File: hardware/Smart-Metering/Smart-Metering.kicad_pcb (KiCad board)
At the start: 4 copper layers, 130 x 130 mm, 227 parts, among them J101 AUX L N, J201 VA VB VC VN, J301 SENSOR_IA, J302 SENSOR_IB, J303 SENSOR_IC, J304 SENSOR_IN, J501 SWD, J701 HMI_LINK, J801 RS485, J802 USB-C, J901 BATTERY_1S, SW901 POWER, U401 ADE9430ACPZ, U501 STM32F413RHT6, U502 24LC64, U601 ISO7762DW, U602 ISO7761DW, U604 MCP3204, U605 TPS7A2033PDBVR, U606 ADuM6000, U801 ADM2587E, U802 USBLC6-2SC6, U901 BQ25895RTW, U902 TPS63001, U903 TPS61022, Y401 24.576MHz, Y501 8MHz, Y502 32.768kHz

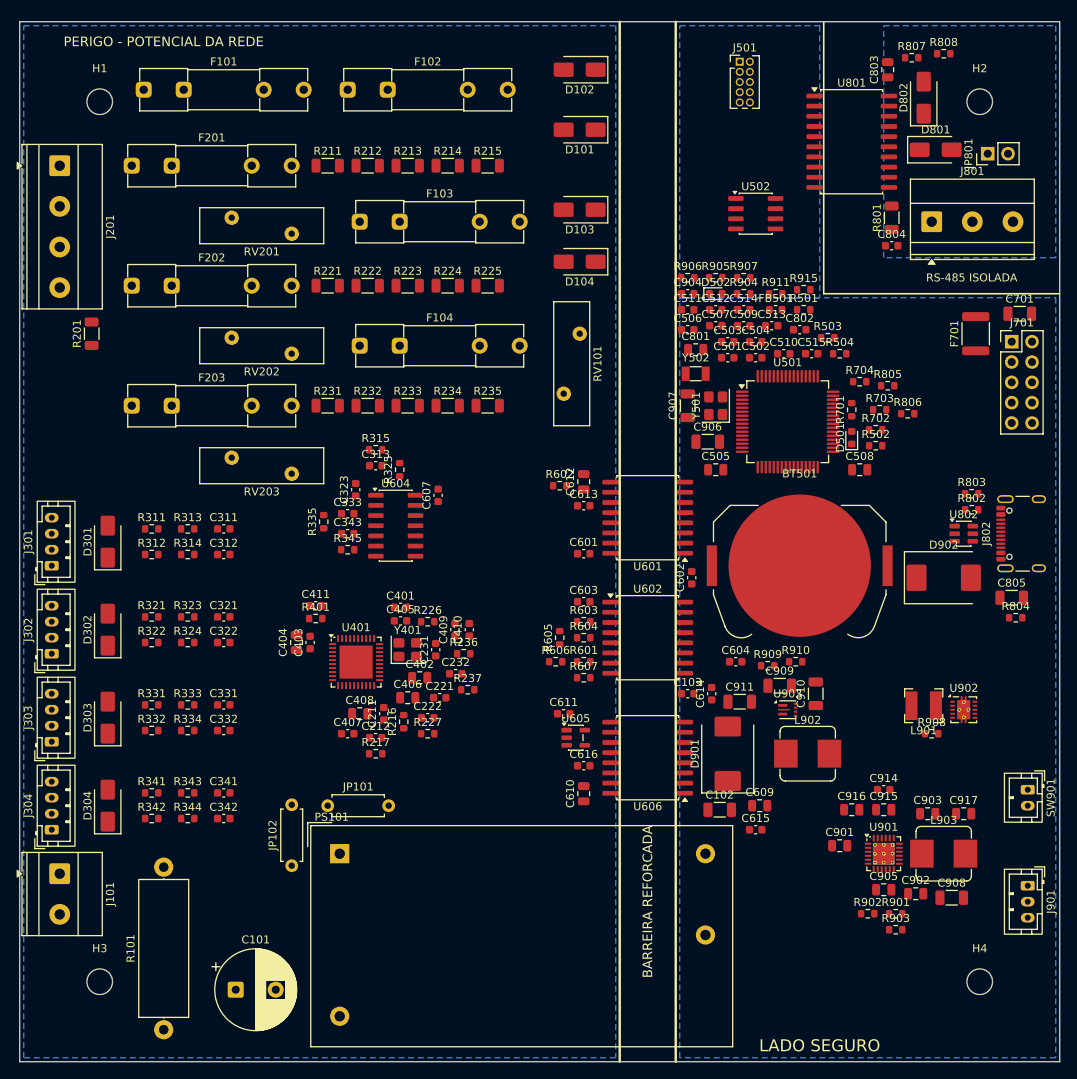
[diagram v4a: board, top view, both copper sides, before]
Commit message: Grava as trilhas e vias do domínio quente na placa
O commit anterior registrou só a documentação; este inclui o roteamento
(3836 trilhas, 139 vias e a zona +3V3_ADE em In2.Cu).

Co-Authored-By: Claude Opus 5.5 <noreply@anthropic.com>
Claude-Session: https://claude.ai/code/session_012B8cVkhtjf3eg98UdpNCpf
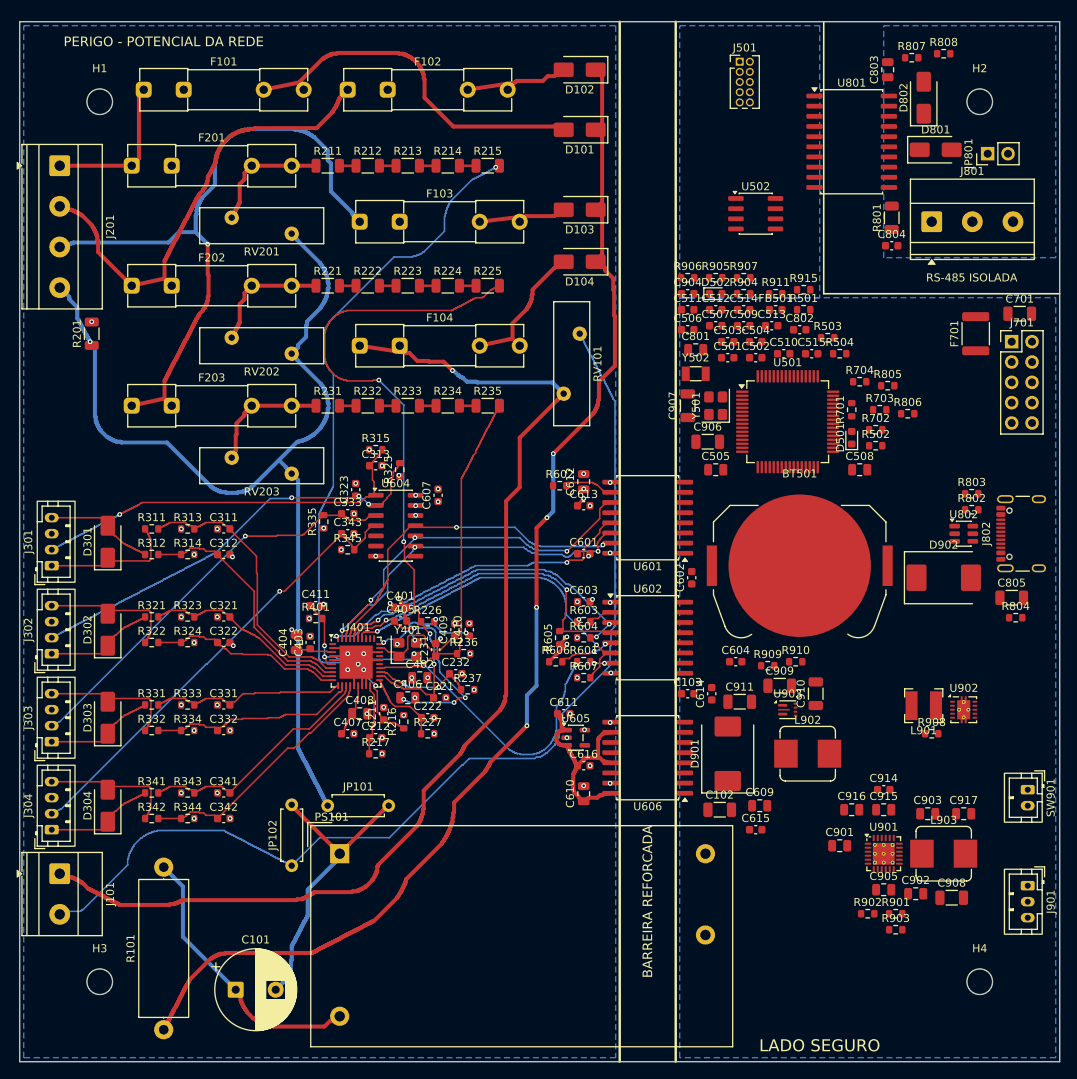
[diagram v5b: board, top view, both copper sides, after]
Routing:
- net Net-(D101-Pad1): track 0.00 -> 155.5 mm, vias 0 -> 4
- net /Power Input/L_AUX: track 0.00 -> 140.3 mm, vias 0 -> 1
- net /Power Input/N_AUX: track 0.00 -> 131.4 mm
- net NEUTRAL: track 0.00 -> 130.6 mm, vias 0 -> 1
- net VAP: track 0.00 -> 91.1 mm, vias 0 -> 2
- net VBP: track 0.00 -> 86.8 mm, vias 0 -> 4
- net LINE_C: track 0.00 -> 83.6 mm, vias 0 -> 1
- net SID_N: track 0.00 -> 57.6 mm, vias 0 -> 1
- net LINE_B: track 0.00 -> 57.6 mm
- net SID_B: track 0.00 -> 55.0 mm, vias 0 -> 3
- net RESET_ADE: track 0.00 -> 54.3 mm, vias 0 -> 3
- net SID_C: track 0.00 -> 51.9 mm, vias 0 -> 1
- net SID_A: track 0.00 -> 49.8 mm, vias 0 -> 1
- net Net-(D101-Pad2): track 0.00 -> 45.0 mm
- net MISO_ADE: track 0.00 -> 44.7 mm, vias 0 -> 3
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- added copper zone on In2.Cu, net +3V3_ADE

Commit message: Liga parte das pendências do domínio quente e alinha CIs de passo fino
- reparo local (com retirada e refação dos nets que bloqueiam): ligados
  SS_SID (U604.8), IRQ0_ADE (U401.31) e +3V3_ADE em U401.1 e U401.27;
  alguns trechos curtos usam In2.Cu (plano +3V3_ADE) como camada de sinal;
- U501, U901, U902, U903 e J802 deslocados até 0,05 mm para os pads de
  passo 0,5 mm ficarem na grade de roteamento (preparação do lado seguro).

Verificação geométrica do domínio quente: 0 violações.

Co-Authored-By: Claude Opus 5.5 <noreply@anthropic.com>
Claude-Session: https://claude.ai/code/session_012B8cVkhtjf3eg98UdpNCpf
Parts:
- moved U901 0.07 mm to (148.1, 134.1)
- moved U501 0.07 mm to (135.9, 80.0)
- moved J802 0.06 mm to (166.3, 94.0)
- moved U903 0.06 mm to (136.0, 116.0)
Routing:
- net IRQ0_ADE: track 6.18 -> 49.4 mm, vias 0 -> 4
- net /Isolation/SS_SID: track 0.00 -> 25.7 mm, vias 0 -> 4
- net RESET_ADE: track 54.3 -> 46.7 mm, vias 3 -> 4
- net +3V3_ADE: track 7.44 -> 9.71 mm, vias 21 -> 23
- added copper zone on In2.Cu, net +3V3

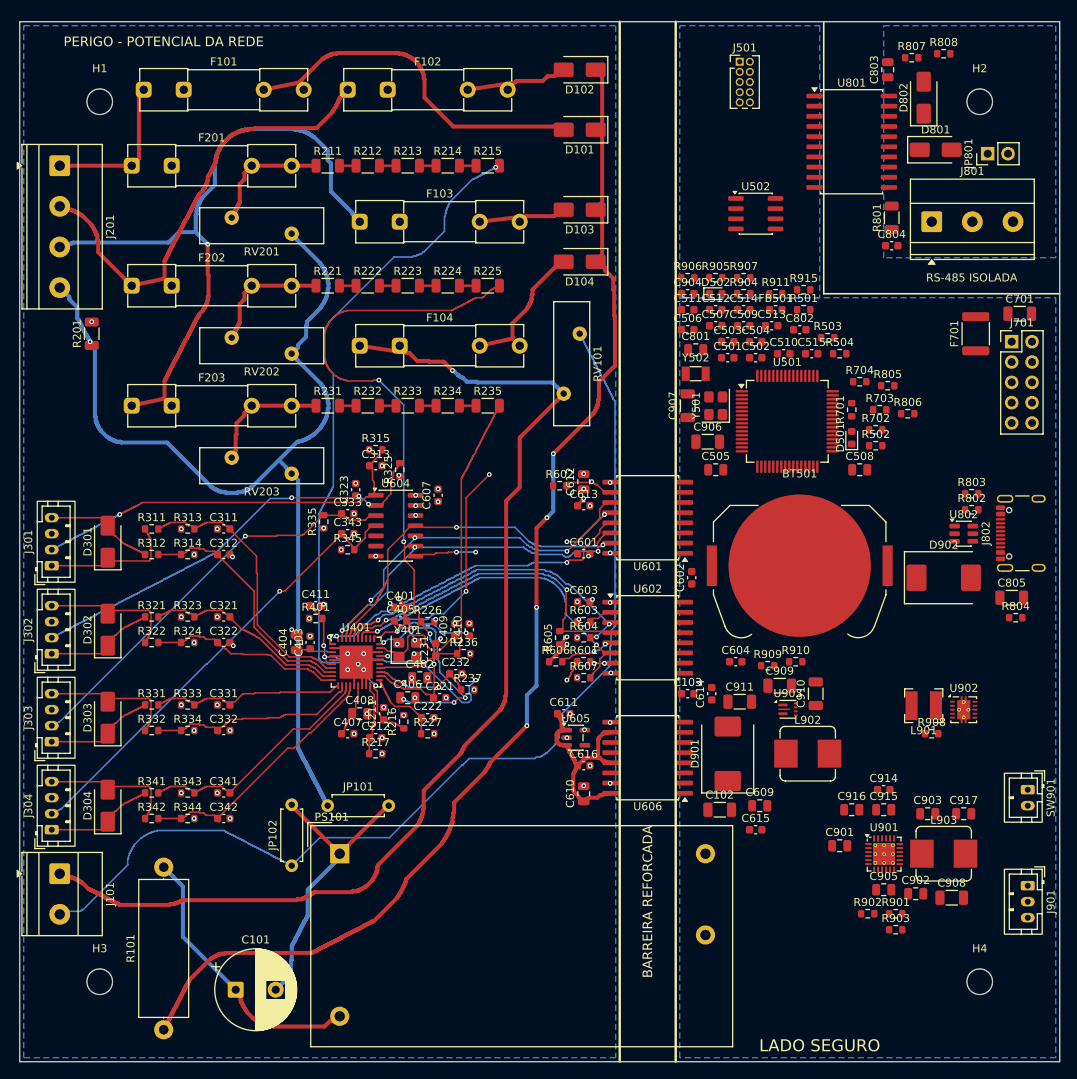
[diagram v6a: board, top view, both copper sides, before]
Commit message: Corrige os achados da revisão automática do PR #1
- BQ25895: divisor do TS invertido (R901 = 5,23 kΩ REGN-TS, R903 = 30,1 kΩ
  TS-GND); antes o carregador via sobretemperatura e não carregava.
- Detecção da fonte: Q902 une D+/D- (DCP, 3 A) só com o AC/DC presente;
  só pelo USB-C a entrada fica em 500 mA. Q901 corta o VBUS quando o AC/DC
  está presente (prioridade do AC/DC sobre a porta USB). R912 polariza os dois.
- DRC: classes DIVIDER_A/B/C, regras entre divisores de fases diferentes
  (3,0 mm), divisor x domínio metrológico (2,0 mm), divisor x rede de outras
  fases (3,0 mm), barramento HV com clearance e creepage, creepage da
  barreira 8,0 mm (com regra própria entre as fileiras dos isoladores).
- Pinos sem uso do lado isolado do U606 classificados no domínio quente.
- Projeto KiCad: folha raiz correta em top_level_sheets.
- PCB: Q901, Q902, R912 posicionados; C103 afastado dos pads quentes de
  U602/U606; zonas com margem para 8 mm na barreira.
- Documentação: ISO7762/ISO7761 na arquitetura, limite de entrada de 3 A
  na revisão, roteamento do domínio quente descrito como parcial.

Co-Authored-By: Claude Opus 5.5 <noreply@anthropic.com>
Claude-Session: https://claude.ai/code/session_012B8cVkhtjf3eg98UdpNCpf
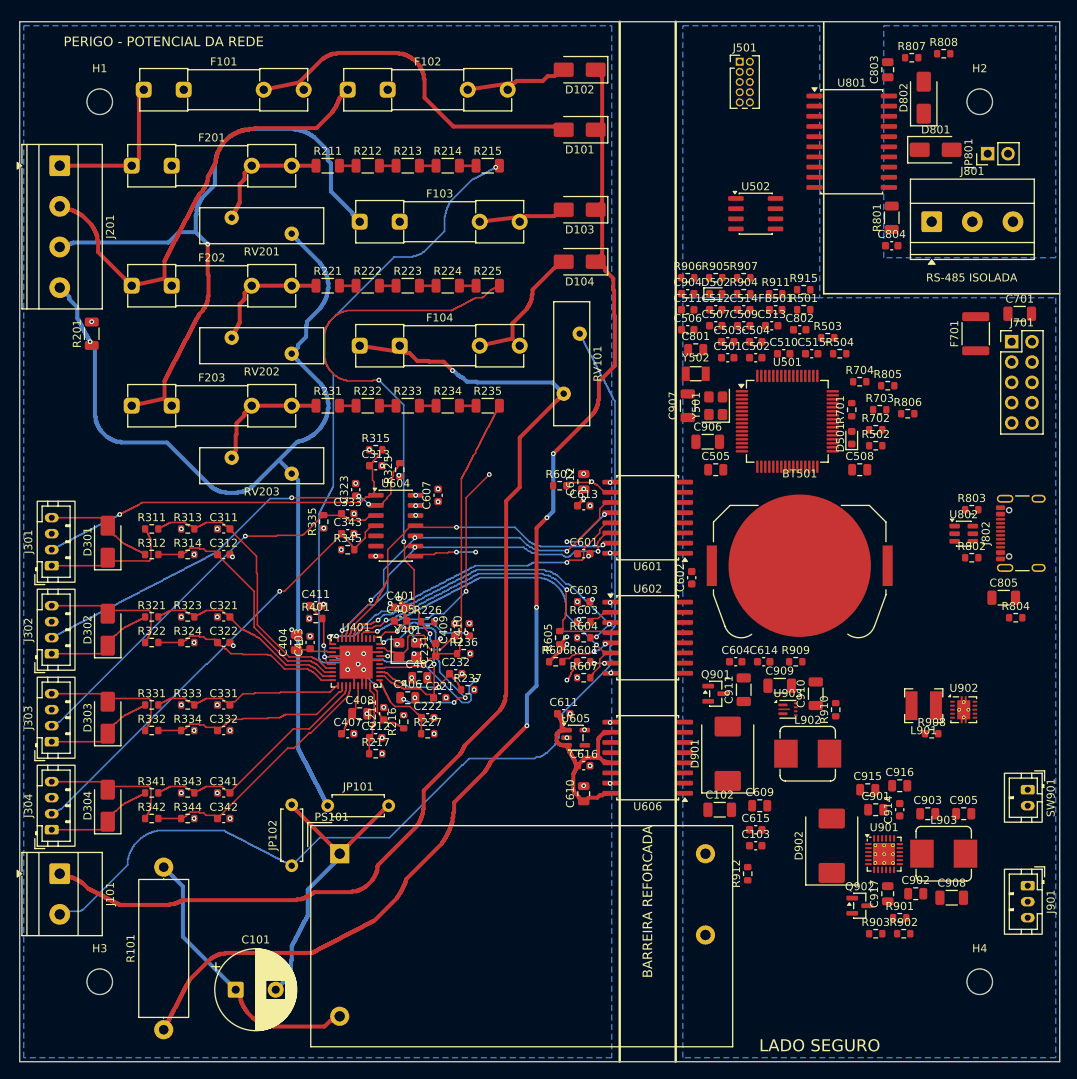
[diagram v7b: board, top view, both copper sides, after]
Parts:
- removed the H1 at (50.0, 40.0)
- added H4: MountingHole_3.2mm_M3, MountingHole:MountingHole_3.2mm_M3, F.Cu at (160.0, 150.0)
- added Q901: AO3401A, Package_TO_SOT_SMD:SOT-23, F.Cu at (127.0, 114.0)
- added Q902: 2N7002, Package_TO_SOT_SMD:SOT-23, F.Cu at (145.0, 140.5)
- added R912: 100k, Resistor_SMD:R_0603_1608Metric, F.Cu at (131.0, 136.5)
- R901: value 30.1k -> 5.23k
- R903: value 5.23k -> 30.1k
- moved H1 155.6 mm to (50.0, 40.0)
- moved D902 36.3 mm to (141.5, 133.0), turned to 90 degrees
- moved C103 20.8 mm to (132.0, 133.0)
- moved C905 13.8 mm to (158.0, 129.0)
- moved C917 13.8 mm to (148.5, 139.0), turned to 90 degrees
- moved R910 7.81 mm to (142.0, 116.0), turned to 90 degrees
- moved C614 7.63 mm to (133.0, 110.0), turned to 0 degrees
- moved C916 6.71 mm to (150.0, 125.5)
- moved C901 6.36 mm to (147.0, 128.5)
- moved R802 6.00 mm to (159.0, 97.0)
- moved R902 5.15 mm to (150.5, 144.0)
- moved R909 3.54 mm to (137.0, 110.0)
- moved C914 3.20 mm to (150.0, 128.5), turned to 90 degrees
- moved C915 3.20 mm to (146.0, 126.0)
- moved R903 2.55 mm to (147.0, 144.0)
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- renumbered H4 to H1
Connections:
- D902 pad 2: VBUS -> /Power Supplies/VBUS_SW
- U901 pad 2: /Power Supplies/CHG_DPDM -> /Power Supplies/CHG_DP
- U901 pad 3: /Power Supplies/CHG_DPDM -> /Power Supplies/CHG_DM

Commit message: Roteia o lado seguro e refaz o domínio quente com creepage de 8 mm
- domínio quente refeito com o cobre até x = 73,65 mm (eixo) e o lado
  seguro a partir de x = 83,2 mm: menor distância quente-seguro através da
  barreira de 8,02 mm (fora as fileiras de pads dos isoladores);
- RV101 2 mm à esquerda (F104 fixado) para abrir a coluna do barramento
  retificado junto da barreira;
- lado seguro e ilha RS-485 roteados: GND_SYS/GND_485 em In1.Cu, +3V3 em
  In2.Cu, trilhas de potência de 0,6 mm estreitadas na saída dos CIs de
  passo fino; In2.Cu usado como camada de sinal em trechos curtos;
- verificação geométrica da placa inteira: 0 violações;
- restam 18 pads para ligar à mão (6 no domínio quente, 12 no lado seguro),
  listados em docs/LAYOUT.md; falta o DRC do KiCad.

Co-Authored-By: Claude Opus 5.5 <noreply@anthropic.com>
Claude-Session: https://claude.ai/code/session_012B8cVkhtjf3eg98UdpNCpf
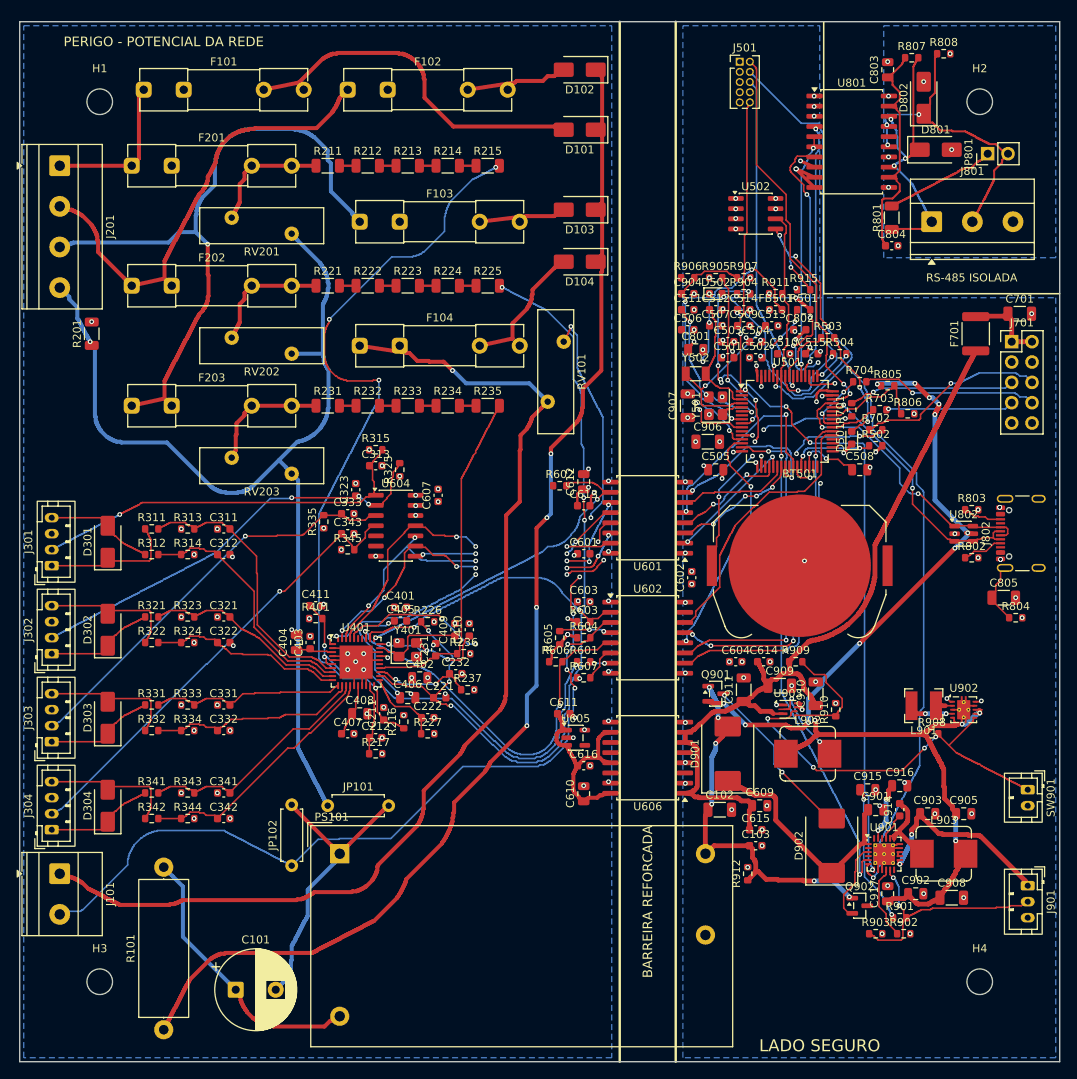
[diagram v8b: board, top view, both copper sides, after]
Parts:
- moved RV101 2.24 mm to (106.0, 77.5)
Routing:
- net I2C_SDA: track 0.00 -> 112.4 mm, vias 0 -> 6
- net +5V: track 0.00 -> 104.3 mm
- net CHG_INT_N: track 0.00 -> 103.6 mm, vias 0 -> 8
- net I2C_SCL: track 0.00 -> 90.2 mm, vias 0 -> 2
- net VBUS: track 0.00 -> 74.1 mm, vias 0 -> 11
- net /Power Supplies/VSYS: track 0.00 -> 68.8 mm, vias 0 -> 6
- net /Metrology MCU/SWDIO: track 0.00 -> 49.2 mm, vias 0 -> 2
- net /Power Supplies/PWR_EN: track 0.00 -> 48.6 mm, vias 0 -> 4
- net VIN_ACDC: track 0.00 -> 47.3 mm, vias 0 -> 6
- net /Metrology MCU/SWCLK: track 0.00 -> 45.0 mm, vias 0 -> 1
- net MCU_ZX: track 0.00 -> 43.3 mm, vias 0 -> 4
- net RS485_TX: track 0.00 -> 42.8 mm, vias 0 -> 5
- net MCU_CF2: track 0.00 -> 42.5 mm, vias 0 -> 2
- net CF1_ADE: track 7.00 -> 49.2 mm
- net /Metrology MCU/SWO: track 0.00 -> 41.5 mm, vias 0 -> 1
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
